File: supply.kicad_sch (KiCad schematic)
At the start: 89 parts, among them J3 DC_SOCKET, U1 AP7330-W5-7, U2 AP7330-W5-7, U3 AP7330-W5-7, U4 AP62301WU-7, U5 AP62301WU-7, U6 AP62301WU-7, U8 NCV51200MNTXG

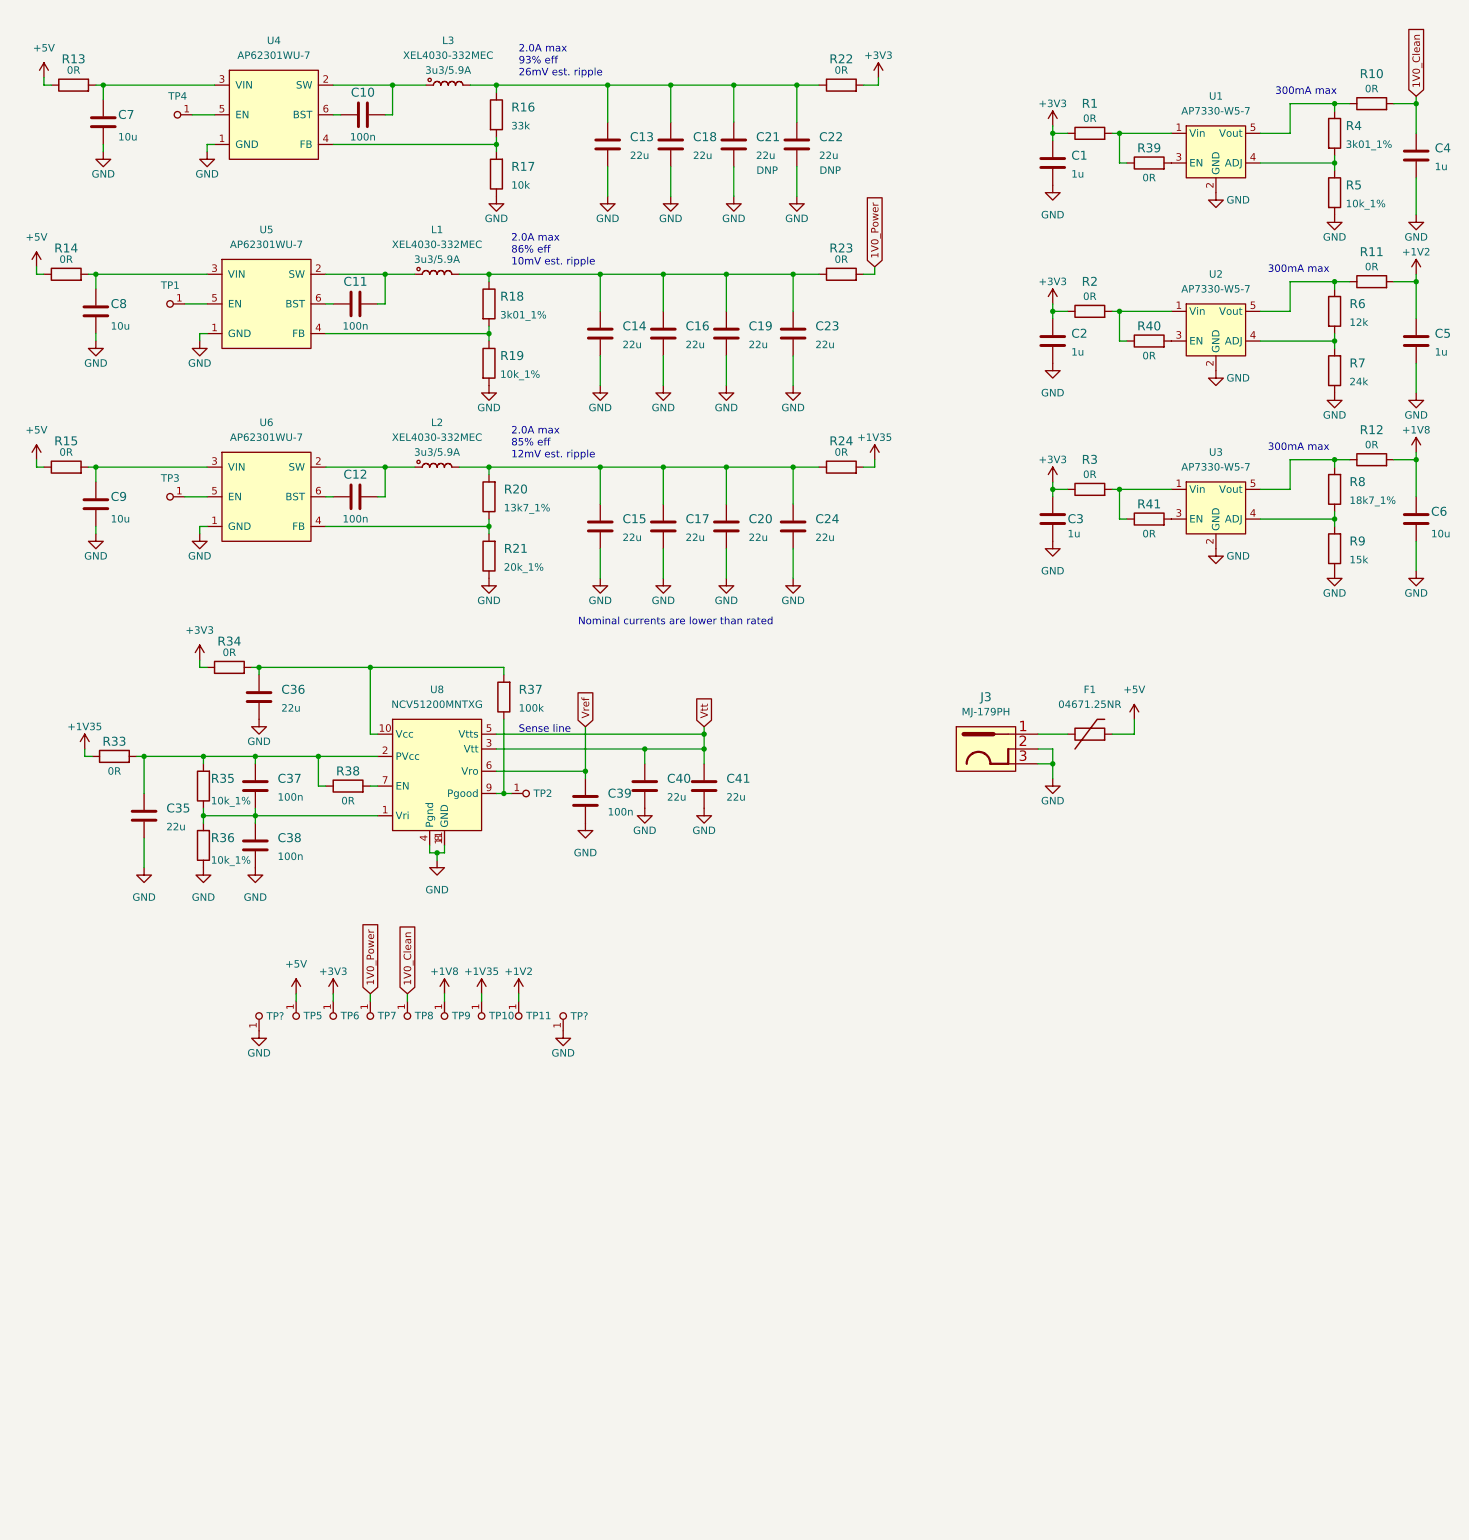
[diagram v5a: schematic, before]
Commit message: Added FPGA configuration circuitry
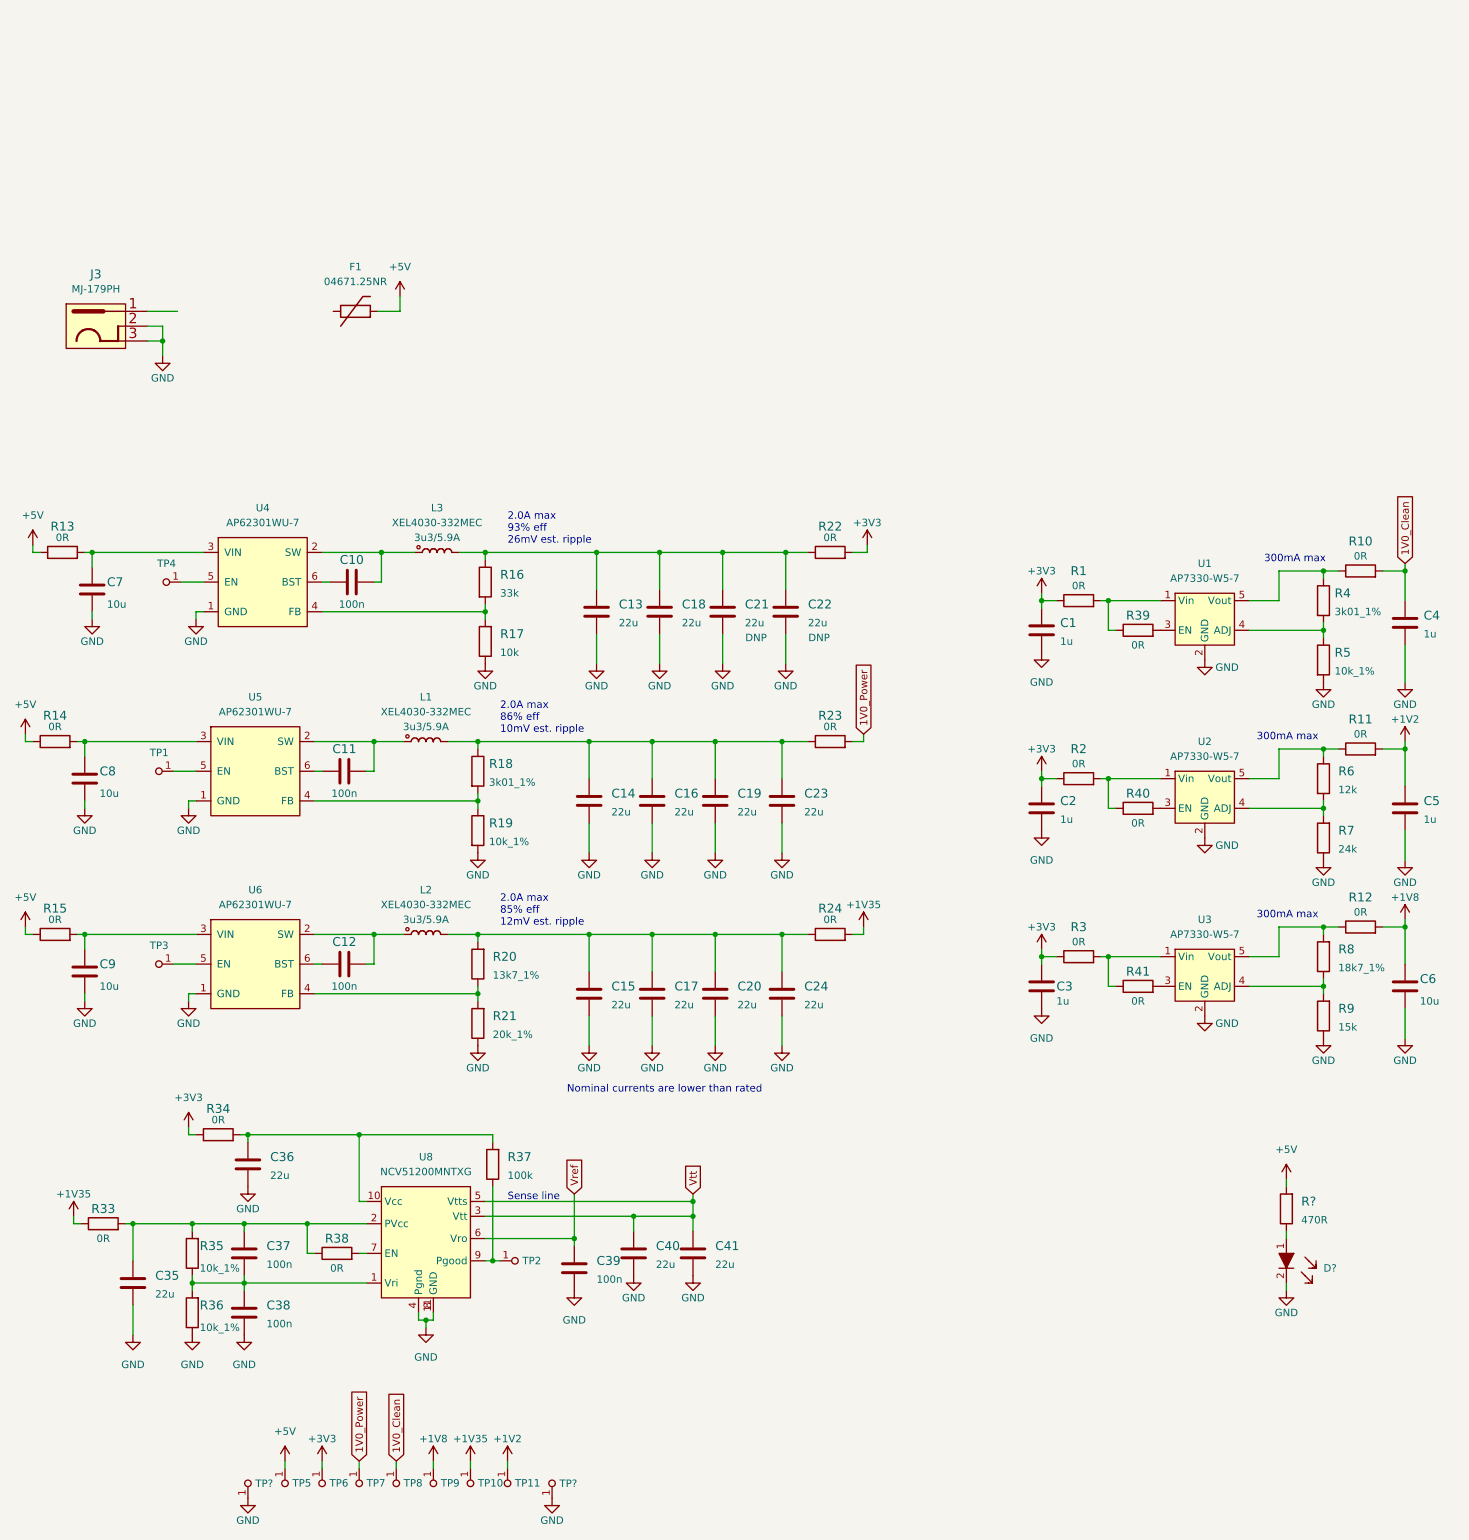
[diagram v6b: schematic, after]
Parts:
- added D?: LTST-C190GKT, antmicro-footprints:LED_0603, symbol antmicroLEDIndicationDiscrete:LTST-C190GKT
- added R?: R_470R_0603, antmicro-footprints:0603-res, symbol antmicroResistors0603:R_470R_0603
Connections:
- net +5V: now also R?.2
- net GND: now also D?.2
- net at J3.1: no longer F1.1
- new net: D?.1, R?.1
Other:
- moved on the sheet: C1, C10, C11, C12, C13, C14, C15, C16, C17, C18, C19, C2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

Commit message: Replaced RPi camera connector with 50pin one, modified PSU with ability of being supplied via FFC
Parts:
- removed F1: 04671.25NR, antmicro-footprints:0603-Fuse-Littelfuse-0467, symbol antmicroFuses:04671.25NR
- added C?: C_10u_0603, antmicro-footprints:0603-cap, symbol antmicroCapacitors0603:C_10u_0603
- added Q? (x3): AO3401A, antmicro-footprints:SOT-23-3, symbol antmicroTransistorsFETsMOSFETsSingle:AO3401A
- added Q? (x2): 2N7002, antmicro-footprints:SOT-23-3, symbol antmicroTransistorsFETsMOSFETsSingle:2N7002
- added R? (x2): R_0R_0805, antmicro-footprints:0805-res, symbol antmicroResistorsmisc:R_0R_0805
- added R? (x2): R_10k_0603, antmicro-footprints:0603-res, symbol antmicroResistors0603:R_10k_0603
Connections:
- net +5V: now also C?.1, R?.2
- net GND: now also C?.2, Q?.2 (S), Q?.2 (S)
- net ALT_5V: now reaches J3.1
- net ALT_5V: now also Q?.1 (G), Q?.3 (D)
- new net: Q?.1 (G), Q?.1 (G), Q?.3 (D), R?.1 (x2)
- new net: Q?.2 (S), Q?.3 (D), R?.1
- new net: Q?.2 (S), Q?.2 (S), R?.2
- new net: Q?.3 (D), R?.2, R?.2
- new net FFC2_5V: R?.1
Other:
- note added: "CONVERTERS"
- note added: "DC jack takes precedence over power via FFC"
- note added: "DDR MEMORY SUPPLY"
- note added: "LDOs"
- note added: "SUPPLY SELECTION"
- note added: "TEST POINTS AND INDICATOR"
- moved on the sheet: C1, C10, C11, C12, C13, C14, C15, C16, C17, C18, C19, C2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

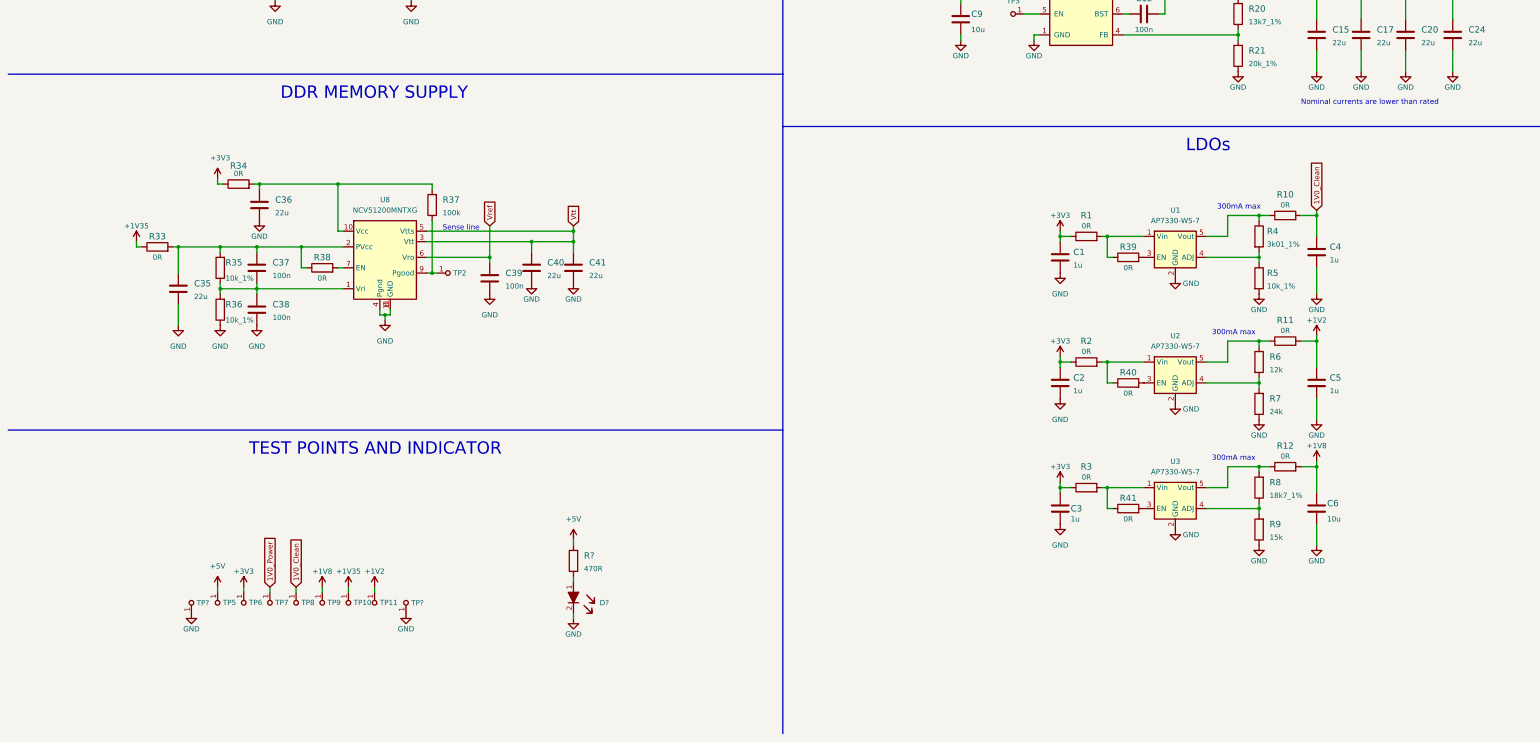
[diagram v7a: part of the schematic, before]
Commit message: Added indicator LEDs and user switch
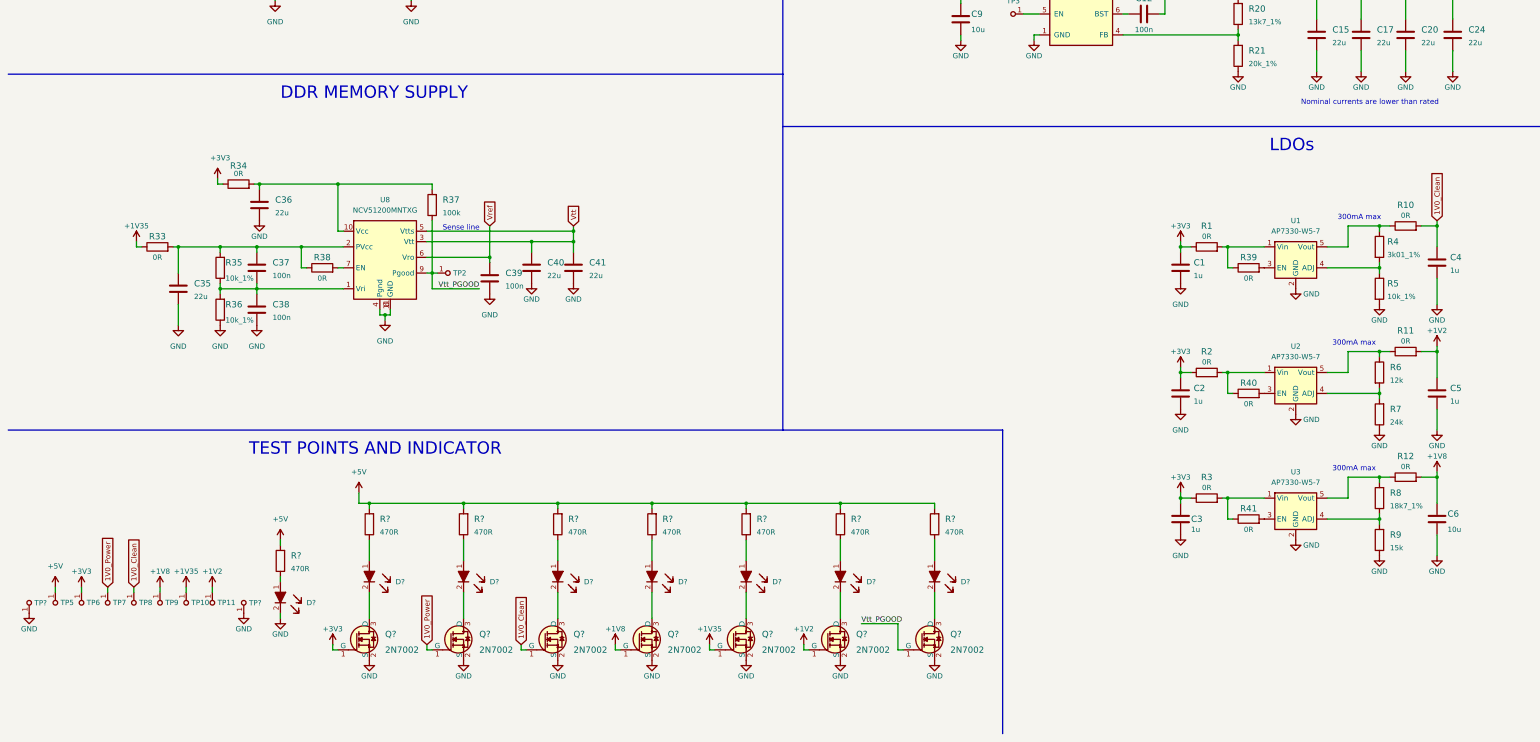
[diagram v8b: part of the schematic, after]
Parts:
- added D? (x7): LTST-C190GKT, antmicro-footprints:LED_0603, symbol antmicroLEDIndicationDiscrete:LTST-C190GKT
- added Q? (x7): 2N7002, antmicro-footprints:SOT-23-3, symbol antmicroTransistorsFETsMOSFETsSingle:2N7002
- added R? (x7): R_470R_0603, antmicro-footprints:0603-res, symbol antmicroResistors0603:R_470R_0603
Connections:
- net +1V2: now also Q?.1 (G)
- net +1V35: now also Q?.1 (G)
- net +1V8: now also Q?.1 (G)
- net +3V3: now also Q?.1 (G)
- net +5V: now also R?.2, R?.2, R?.2, R?.2, R?.2, R?.2, R?.2
- net 1V0_Clean: now also Q?.1 (G)
- net 1V0_Power: now also Q?.1 (G)
- net GND: now also Q?.2 (S), Q?.2 (S), Q?.2 (S), Q?.2 (S), Q?.2 (S), Q?.2 (S), Q?.2 (S)
- net Vtt_PGOOD: now reaches R37.1, TP2.1, U8.9 (Pgood)
- net Vtt_PGOOD: now also Q?.1 (G)
- new net: D?.1, R?.1 (x7)
- new net: D?.2, Q?.3 (D) (x7)
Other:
- moved on the sheet: C1, C2, C3, C4, C5, C6, D?, R1, R10, R11, R12, R2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
